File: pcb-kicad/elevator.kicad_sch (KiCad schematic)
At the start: 154 parts, among them Q1 AO3416, SW1 MX-with-LED, SW10 MX-with-LED, SW11 MX-with-LED, SW12 MX-with-LED, SW13 MX-with-LED, SW14 MX-with-LED, SW15 MX-with-LED, SW16 MX-with-LED, SW17 MX-with-LED, SW18 MX-with-LED, SW19 MX-with-LED, SW2 MX-with-LED, SW20 MX-with-LED, SW21 MX-with-LED, SW22 MX-with-LED, SW23 MX-with-LED, SW24 MX-with-LED, SW25 MX-with-LED, SW26 MX-with-LED, SW27 MX-with-LED, SW28 MX-with-LED, SW29 MX-with-LED, SW3 MX-with-LED, SW30 MX-with-LED, SW31 MX-with-LED, SW32 MX-with-LED, SW33 MX-with-LED, SW34 MX-with-LED, SW35 MX-with-LED, SW36 MX-with-LED, SW37 MX-with-LED, SW38 MX-with-LED, SW39 MX-with-LED, SW4 MX-with-LED, SW40 MX-with-LED, SW41 MX-with-LED, SW42 MX-with-LED, SW43 MX-with-LED, SW44 MX-with-LED, SW45 MX-with-LED, SW46 MX-with-LED, SW47 MX-with-LED, SW48 MX-with-LED, SW49 RotaryEncoder_Switch, SW5 MX-with-LED, SW6 MX-with-LED, SW7 MX-with-LED, SW8 MX-with-LED, SW9 MX-with-LED, U1 Frood

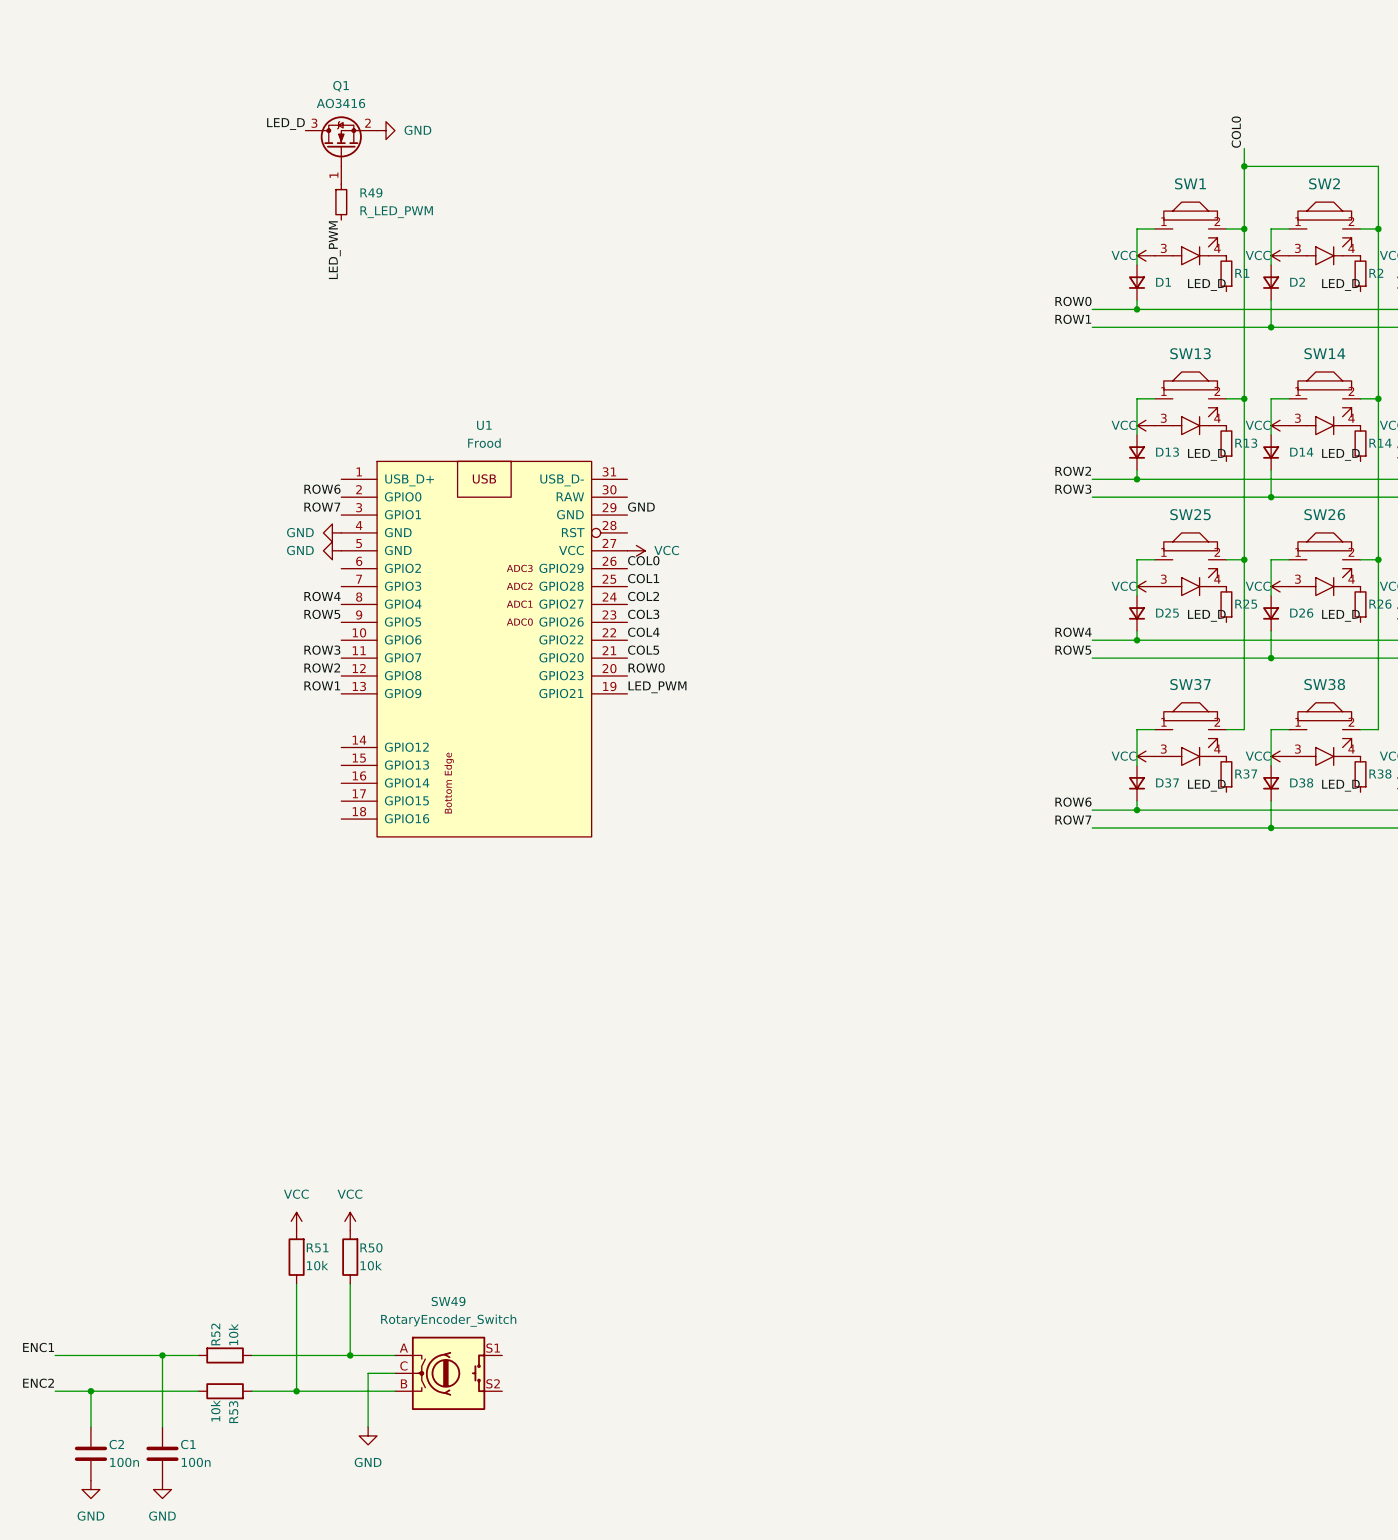
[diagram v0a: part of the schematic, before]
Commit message: Add rotary encoder circuitry to the PCB
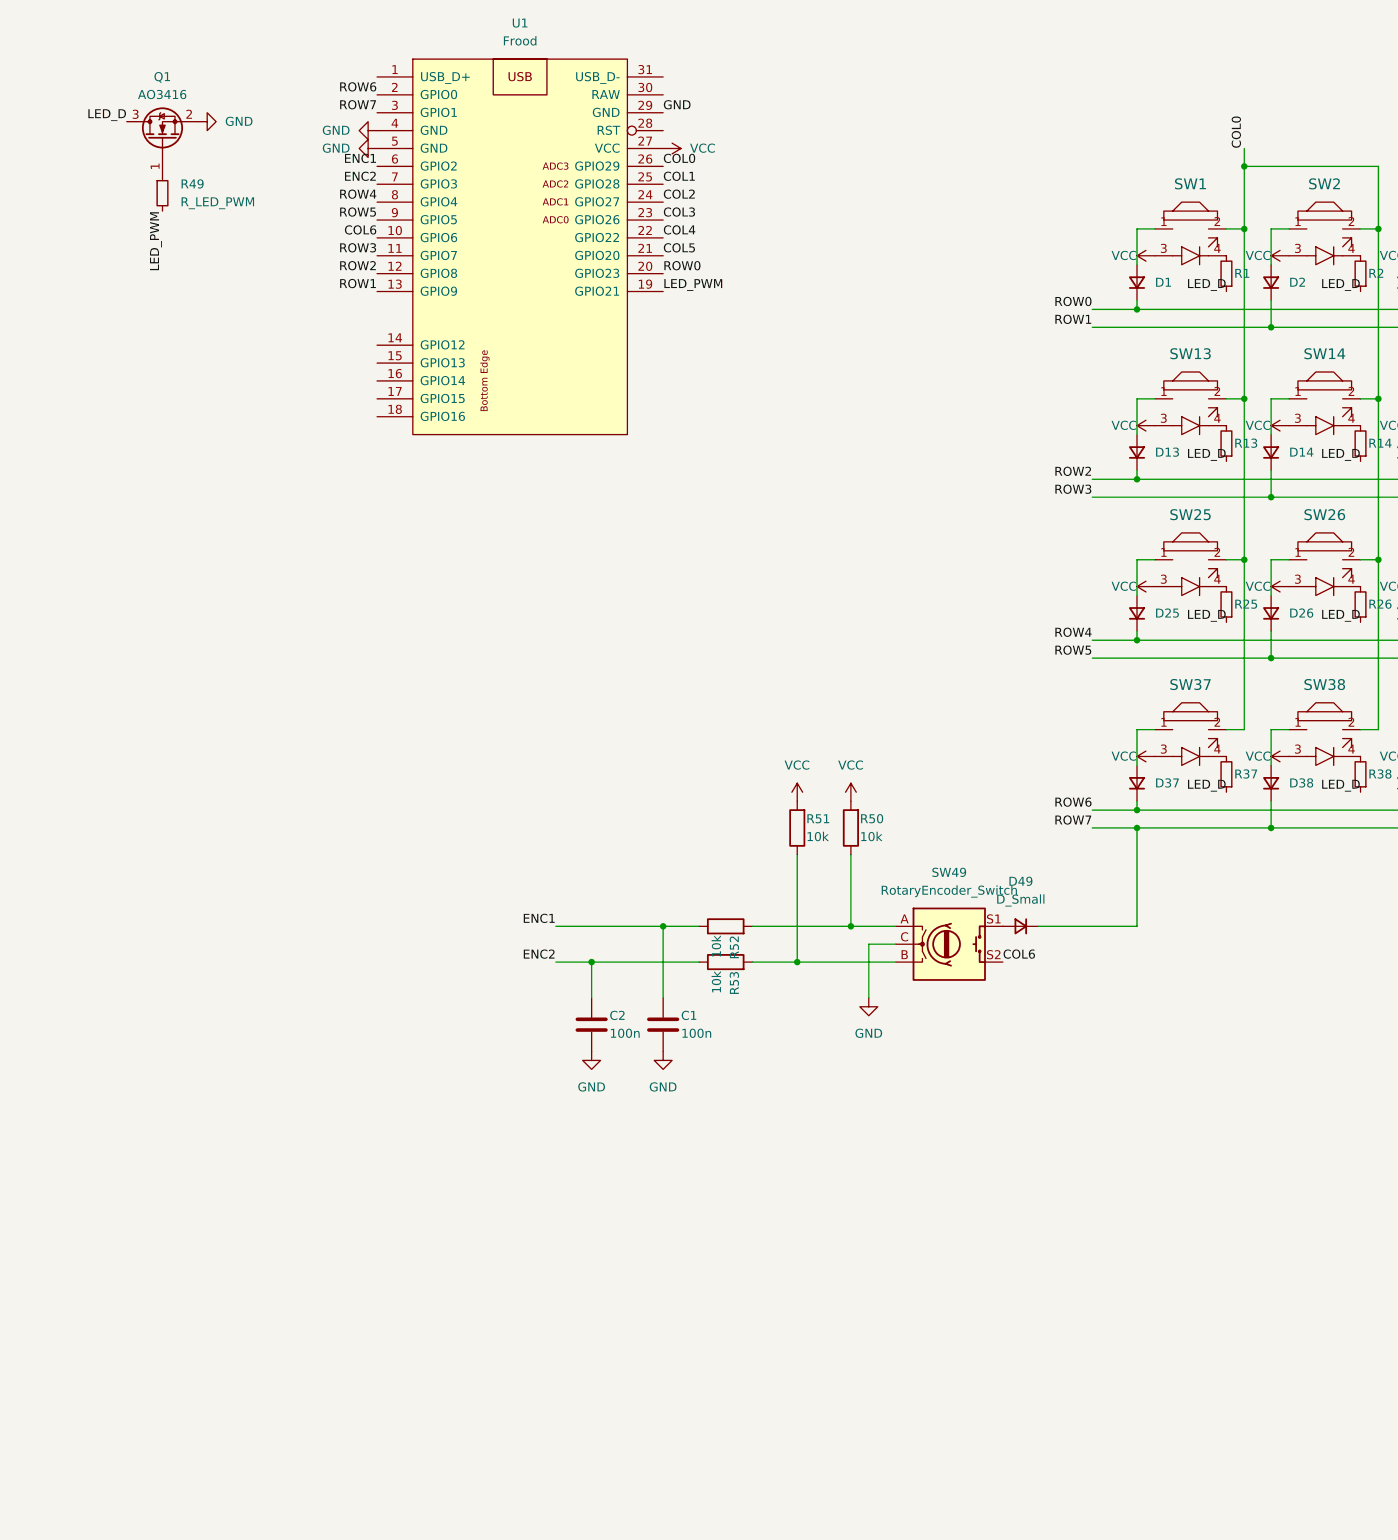
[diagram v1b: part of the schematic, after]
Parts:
- added D49: D_Small, Keebio-Parts:Diode-dual, symbol Device:D_Small
- C1, C2: footprint (none) -> Capacitor_THT:C_Disc_D4.3mm_W1.9mm_P5.00mm
- R50, R51, R52, R53: footprint (none) -> Keebio-Parts:Resistor-Hybrid
- SW49: footprint (none) -> Rotary_Encoder:RotaryEncoder_Alps_EC11E-Switch_Vertical_H20mm
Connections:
- net ENC1: now also R52.1, U1.6 (GPIO2); no longer R52.2
- net ENC2: now also U1.7 (GPIO3)
- net ROW7: now also D49.1 (K)
- net at R50.1, SW49.A: now also R52.2; no longer R52.1
- net COL6: now reaches U1.10 (GPIO6)
- net COL6: now also SW49.S2
- net at SW49.S1: now also D49.2 (A)
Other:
- moved on the sheet: C1, C2, Q1, R49, R50, R51, R52, R53, SW49, U1
